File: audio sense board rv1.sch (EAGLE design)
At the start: 33 parts, among them IC2 TSOP38238, J1 PJRAN1X1U01X, J2 PJRAN1X1U01X, Q1 2N3904, Q2 2N3904

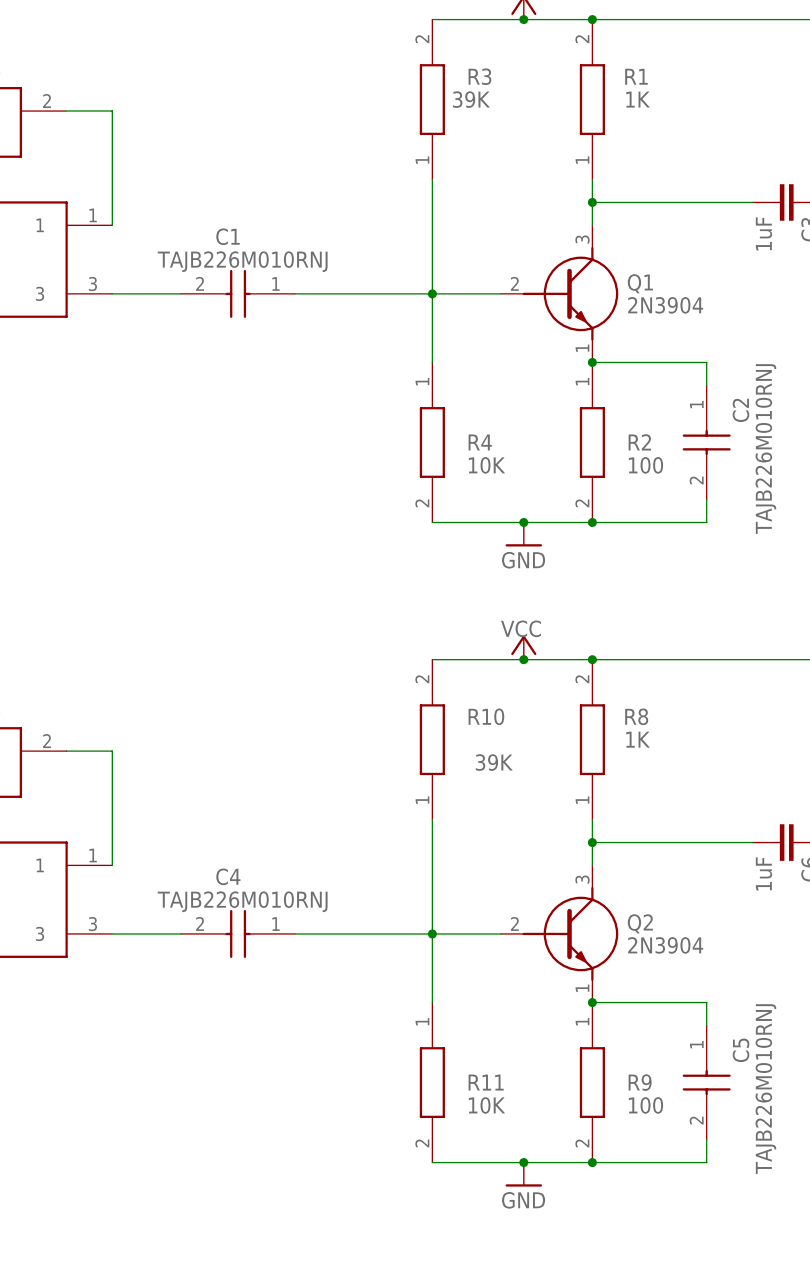
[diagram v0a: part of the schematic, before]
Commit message: fix critical short on R4, overlaps and wire stubs
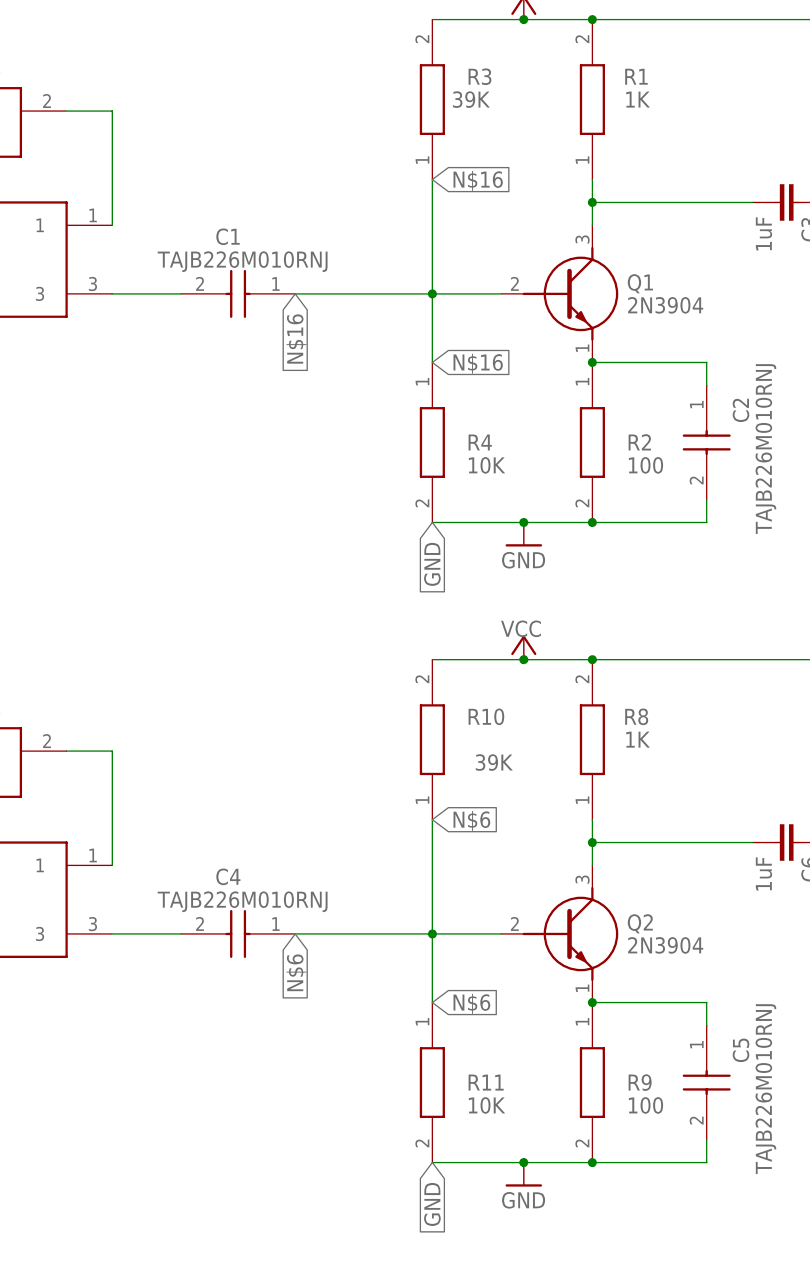
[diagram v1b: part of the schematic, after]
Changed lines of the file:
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@@
 <pinref part="C2" gate="G$1" pin="-"/>
 <wire x1="30.48" y1="33.02" x2="30.48" y2="35.56" width="0.1524" layer="91"/>
+<label x="0" y="33.02" size="1.778" layer="95" rot="R270" xref="yes"/>
 </segment>
 <segment>
@@
 <pinref part="C5" gate="G$1" pin="-"/>
 <wire x1="30.48" y1="-38.1" x2="30.48" y2="-35.56" width="0.1524" layer="91"/>
+<label x="0" y="-38.1" size="1.778" layer="95" rot="R270" xref="yes"/>
 </segment>
 <segment>
@@
 <pinref part="R4" gate="G$1" pin="1"/>
 <wire x1="0" y1="50.8" x2="0" y2="58.42" width="0.1524" layer="91"/>
+<label x="0" y="50.8" size="1.778" layer="95" xref="yes"/>
+<label x="-15.24" y="58.42" size="1.778" layer="95" rot="R270" xref="yes"/>
+<label x="0" y="71.12" size="1.778" layer="95" xref="yes"/>
 </segment>
 </net>
@@
 <pinref part="R11" gate="G$1" pin="1"/>
 <wire x1="0" y1="-20.32" x2="0" y2="-12.7" width="0.1524" layer="91"/>
-</segment>
-</net>
+<label x="0" y="-20.32" size="1.778" layer="95" xref="yes"/>
+<label x="0" y="0" size="1.778" layer="95" xref="yes"/>
+<label x="-15.24" y="-12.7" size="1.778" layer="95" rot="R270" xref="yes"/>
+</segment>
+</net>

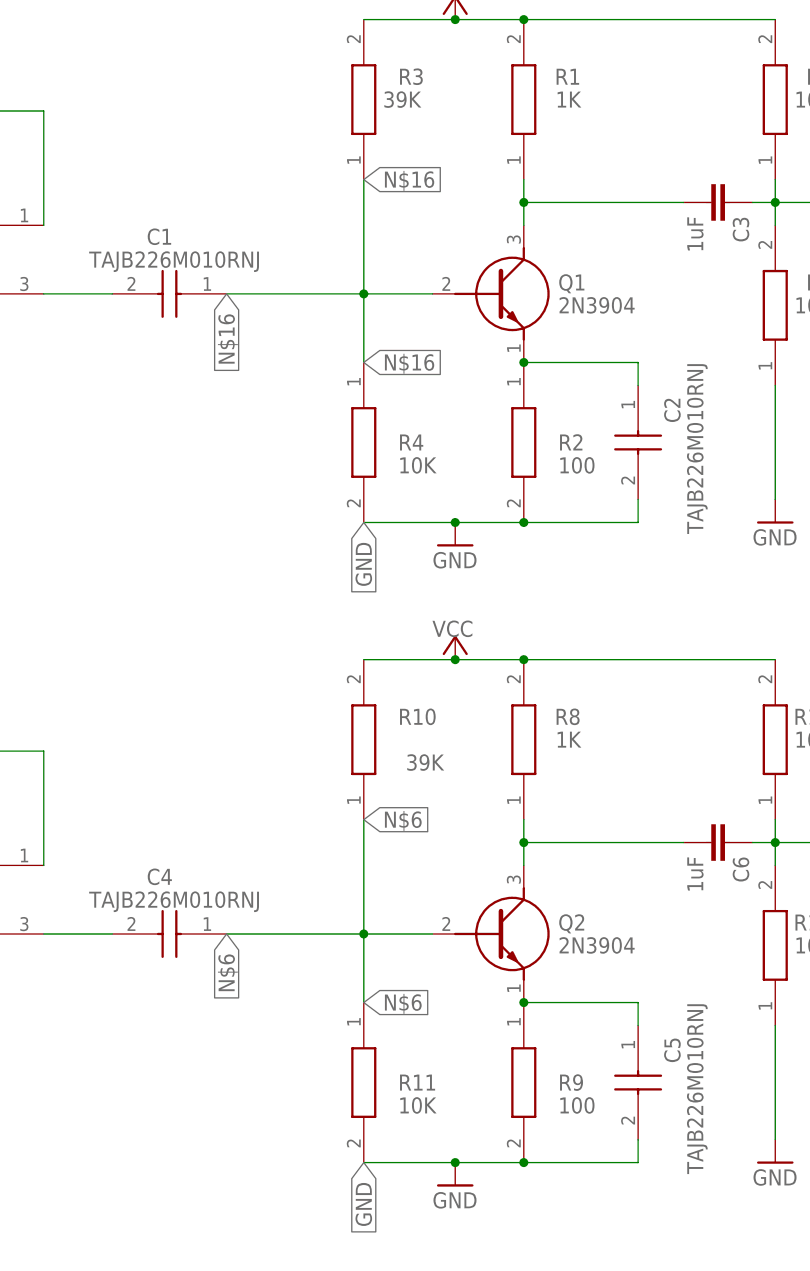
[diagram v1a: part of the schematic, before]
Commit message: increase pad size for all resistors
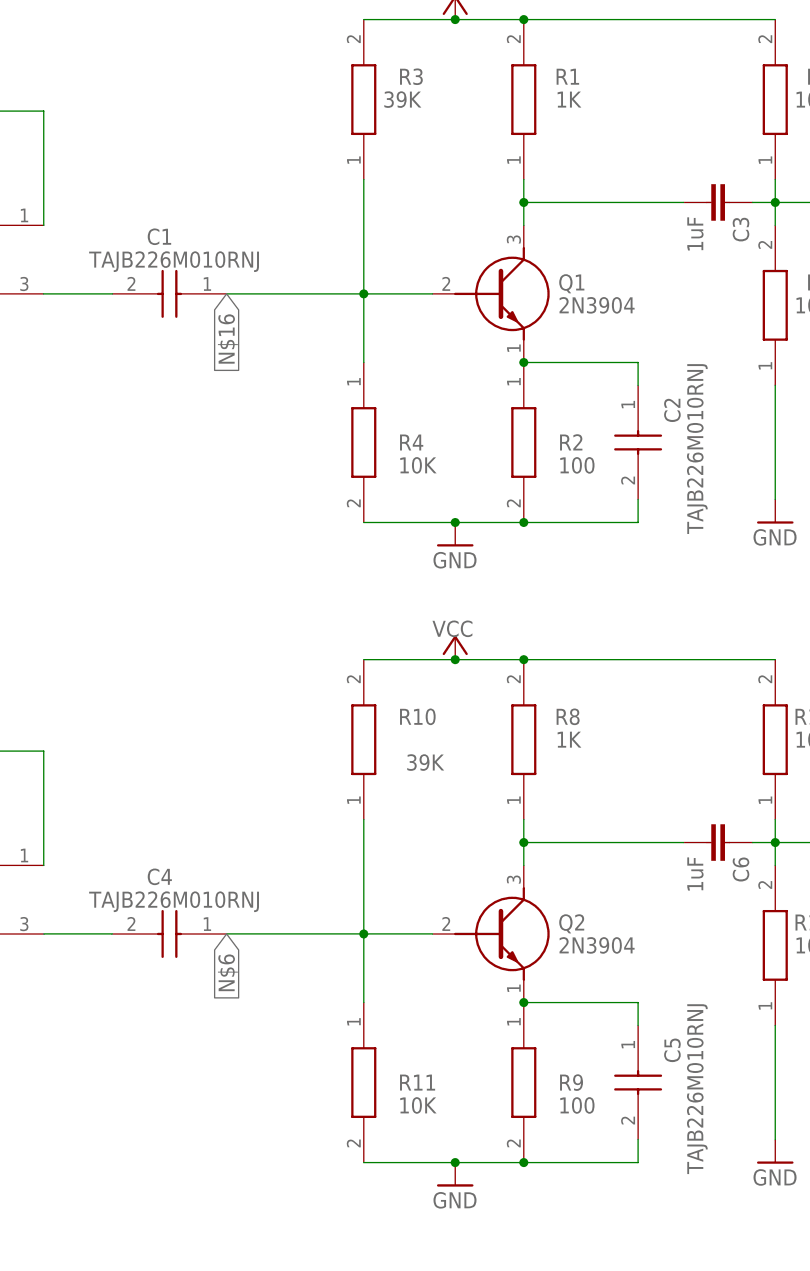
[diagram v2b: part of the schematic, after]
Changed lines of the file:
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@@
 <grid distance="0.1" unitdist="inch" unit="inch" style="lines" multiple="1" display="no" altdistance="0.01" altunitdist="inch" altunit="inch"/>
 <layers>
-<layer number="1" name="Top" color="4" fill="1" visible="no" active="no"/>
-<layer number="16" name="Bottom" color="1" fill="1" visible="no" active="no"/>
-<layer number="17" name="Pads" color="2" fill="1" visible="no" active="no"/>
-<layer number="18" name="Vias" color="2" fill="1" visible="no" active="no"/>
-<layer number="19" name="Unrouted" color="6" fill="1" visible="no" active="no"/>
-<layer number="20" name="Dimension" color="24" fill="1" visible="no" active="no"/>
-<layer number="21" name="tPlace" color="7" fill="1" visible="no" active="no"/>
-<layer number="22" name="bPlace" color="7" fill="1" visible="no" active="no"/>
-<layer number="23" name="tOrigins" color="15" fill="1" visible="no" active="no"/>
-<layer number="24" name="bOrigins" color="15" fill="1" visible="no" active="no"/>
-<layer number="25" name="tNames" color="7" fill="1" visible="no" active="no"/>
-<layer number="26" name="bNames" color="7" fill="1" visible="no" active="no"/>
-<layer number="27" name="tValues" color="7" fill="1" visible="no" active="no"/>
-<layer number="28" name="bValues" color="7" fill="1" visible="no" active="no"/>
+<layer number="1" name="Top" color="4" fill="1" visible="yes" active="no"/>
+<layer number="16" name="Bottom" color="1" fill="1" visible="yes" active="no"/>
+<layer number="17" name="Pads" color="2" fill="1" visible="yes" active="no"/>
+<layer number="18" name="Vias" color="2" fill="1" visible="yes" active="no"/>
+<layer number="19" name="Unrouted" color="6" fill="1" visible="yes" active="no"/>
+<layer number="20" name="Dimension" color="24" fill="1" visible="yes" active="no"/>
+<layer number="21" name="tPlace" color="7" fill="1" visible="yes" active="no"/>
+<layer number="22" name="bPlace" color="7" fill="1" visible="yes" active="no"/>
+<layer number="23" name="tOrigins" color="15" fill="1" visible="yes" active="no"/>
+<layer number="24" name="bOrigins" color="15" fill="1" visible="yes" active="no"/>
+<layer number="25" name="tNames" color="7" fill="1" visible="yes" active="no"/>
+<layer number="26" name="bNames" color="7" fill="1" visible="yes" active="no"/>
+<layer number="27" name="tValues" color="7" fill="1" visible="yes" active="no"/>
+<layer number="28" name="bValues" color="7" fill="1" visible="yes" active="no"/>
 <layer number="29" name="tStop" color="7" fill="3" visible="no" active="no"/>
 <layer number="30" name="bStop" color="7" fill="6" visible="no" active="no"/>
@@
 <layer number="35" name="tGlue" color="7" fill="4" visible="no" active="no"/>
 <layer number="36" name="bGlue" color="7" fill="5" visible="no" active="no"/>
-<layer number="37" name="tTest" color="7" fill="1" visible="no" active="no"/>
-<layer number="38" name="bTest" color="7" fill="1" visible="no" active="no"/>
+<layer number="37" name="tTest" color="7" fill="1" visible="yes" active="no"/>
+<layer number="38" name="bTest" color="7" fill="1" visible="yes" active="no"/>
 <layer number="39" name="tKeepout" color="4" fill="11" visible="no" active="no"/>
 <layer number="40" name="bKeepout" color="1" fill="11" visible="no" active="no"/>
@@
 <layer number="44" name="Drills" color="7" fill="1" visible="no" active="no"/>
 <layer number="45" name="Holes" color="7" fill="1" visible="no" active="no"/>
-<layer number="46" name="Milling" color="3" fill="1" visible="no" active="no"/>
-<layer number="47" name="Measures" color="7" fill="1" visible="no" active="no"/>
-<layer number="48" name="Document" color="7" fill="1" visible="no" active="no"/>
-<layer number="49" name="Reference" color="7" fill="1" visible="no" active="no"/>
-<layer number="50" name="dxf" color="7" fill="1" visible="no" active="no"/>
-<layer number="51" name="tDocu" color="7" fill="1" visible="no" active="no"/>
-<layer number="52" name="bDocu" color="7" fill="1" visible="no" active="no"/>
-<layer number="53" name="tGND_GNDA" color="7" fill="9" visible="no" active="no"/>
-<layer number="54" name="bGND_GNDA" color="1" fill="9" visible="no" active="no"/>
-<layer number="56" name="wert" color="7" fill="1" visible="no" active="no"/>
-<layer number="57" name="tCAD" color="7" fill="1" visible="no" active="no"/>
-<layer number="59" name="tCarbon" color="7" fill="1" visible="no" active="no"/>
-<layer number="60" name="bCarbon" color="7" fill="1" visible="no" active="no"/>
+<layer number="46" name="Milling" color="3" fill="1" visible="yes" active="no"/>
+<layer number="47" name="Measures" color="7" fill="1" visible="yes" active="no"/>
+<layer number="48" name="Document" color="7" fill="1" visible="yes" active="no"/>
+<layer number="49" name="Reference" color="7" fill="1" visible="yes" active="no"/>
+<layer number="50" name="dxf" color="7" fill="1" visible="yes" active="no"/>
+<layer number="51" name="tDocu" color="7" fill="1" visible="yes" active="no"/>
+<layer number="52" name="bDocu" color="7" fill="1" visible="yes" active="no"/>
+<layer number="53" name="tGND_GNDA" color="7" fill="9" visible="yes" active="no"/>
+<layer number="54" name="bGND_GNDA" color="1" fill="9" visible="yes" active="no"/>
+<layer number="56" name="wert" color="7" fill="1" visible="yes" active="no"/>
+<layer number="57" name="tCAD" color="7" fill="1" visible="yes" active="no"/>
+<layer number="59" name="tCarbon" color="7" fill="1" visible="yes" active="no"/>
+<layer number="60" name="bCarbon" color="7" fill="1" visible="yes" active="no"/>
 <layer number="88" name="SimResults" color="9" fill="1" visible="yes" active="yes"/>
 <layer number="89" name="SimProbes" color="9" fill="1" visible="yes" active="yes"/>
@@
 <pinref part="C2" gate="G$1" pin="-"/>
 <wire x1="30.48" y1="33.02" x2="30.48" y2="35.56" width="0.1524" layer="91"/>
-<label x="0" y="33.02" size="1.778" layer="95" rot="R270" xref="yes"/>
 </segment>
 <segment>
@@
 <pinref part="C5" gate="G$1" pin="-"/>
 <wire x1="30.48" y1="-38.1" x2="30.48" y2="-35.56" width="0.1524" layer="91"/>
-<label x="0" y="-38.1" size="1.778" layer="95" rot="R270" xref="yes"/>
 </segment>
 <segment>
@@
 <pinref part="R4" gate="G$1" pin="1"/>
 <wire x1="0" y1="50.8" x2="0" y2="58.42" width="0.1524" layer="91"/>
-<label x="0" y="50.8" size="1.778" layer="95" xref="yes"/>
 <label x="-15.24" y="58.42" size="1.778" layer="95" rot="R270" xref="yes"/>
-<label x="0" y="71.12" size="1.778" layer="95" xref="yes"/>
 </segment>
 </net>
@@
 <pinref part="R11" gate="G$1" pin="1"/>
 <wire x1="0" y1="-20.32" x2="0" y2="-12.7" width="0.1524" layer="91"/>
-<label x="0" y="-20.32" size="1.778" layer="95" xref="yes"/>
-<label x="0" y="0" size="1.778" layer="95" xref="yes"/>
 <label x="-15.24" y="-12.7" size="1.778" layer="95" rot="R270" xref="yes"/>
 </segment>
